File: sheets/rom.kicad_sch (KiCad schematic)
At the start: 3 parts, among them U34 NEO-E0, U35 74LS259, U36 27C1024

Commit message: Updated Footprints
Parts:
- U34: footprint (none) -> Package_LCC:PLCC-84
- U35: footprint (none) -> Package_DIP:DIP-16_W7.62mm
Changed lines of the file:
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@@
       (effects (font (size 1.27 1.27)) (justify left))
     )
-    (property "Footprint" "" (id 2) (at 156.21 93.218 0)
+    (property "Footprint" "Package_DIP:DIP-16_W7.62mm" (id 2) (at 156.21 93.218 0)
       (effects (font (size 1.27 1.27)) hide)
     )
@@
     (property "Reference" "U34" (id 0) (at 245.491 76.454 0))
     (property "Value" "NEO-E0" (id 1) (at 253.746 170.434 0))
-    (property "Footprint" "" (id 2) (at 253.746 136.144 0)
+    (property "Footprint" "Package_LCC:PLCC-84" (id 2) (at 253.746 136.144 0)
       (effects (font (size 1.27 1.27)) hide)
     )

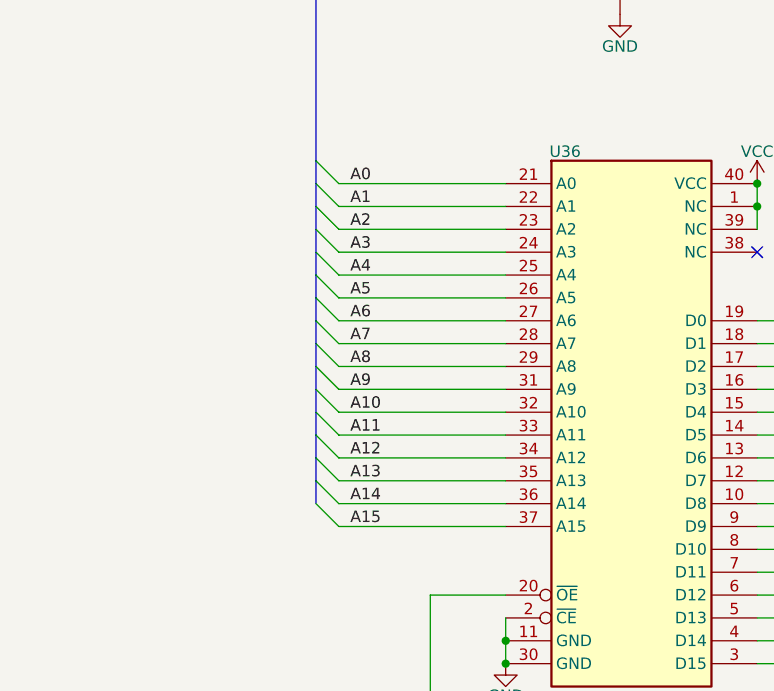
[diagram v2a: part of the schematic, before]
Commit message: Fix 27c1024 wrong address map
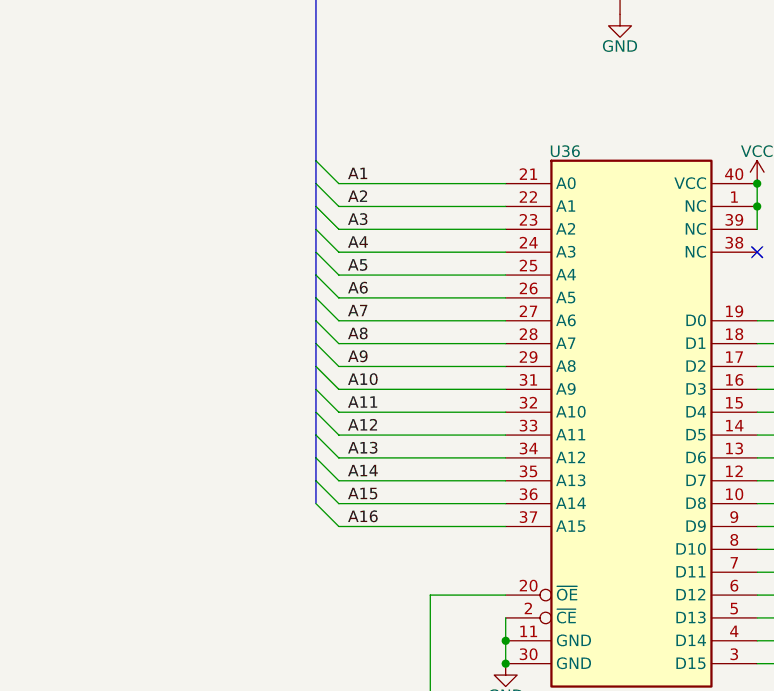
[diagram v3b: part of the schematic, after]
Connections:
- net A0 is gone; now on net A1: U36.21 (A0)
- net A1: no longer U36.22 (A1)
- net A10: now also U36.31 (A9); no longer U36.32 (A10)
- net A11: now also U36.32 (A10); no longer U36.33 (A11)
- net A12: now also U36.33 (A11); no longer U36.34 (A12)
- net A13: now also U36.34 (A12); no longer U36.35 (A13)
- net A14: now also U36.35 (A13); no longer U36.36 (A14)
- net A15: now also U36.36 (A14); no longer U36.37 (A15)
- net A16: now also U36.37 (A15)
- net A2: now also U36.22 (A1); no longer U36.23 (A2)
- net A3: now also U36.23 (A2); no longer U36.24 (A3)
- net A4: now also U36.24 (A3); no longer U36.25 (A4)
- net A5: now also U36.25 (A4); no longer U36.26 (A5)
- net A6: now also U36.26 (A5); no longer U36.27 (A6)
- net A7: now also U36.27 (A6); no longer U36.28 (A7)
- net A8: now also U36.28 (A7); no longer U36.29 (A8)
- net A9: now also U36.29 (A8); no longer U36.31 (A9)
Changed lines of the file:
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@@
     (stroke (width 0) (type default) (color 0 0 0 0))
   )
-  (label "A5" (at 126.238 142.494 0)
+  (label "A5" (at 125.984 139.954 0)
     (effects (font (size 1.27 1.27)) (justify left bottom))
   )
@@
     (effects (font (size 1.27 1.27)) (justify right bottom))
   )
-  (label "A2" (at 126.238 134.874 0)
+  (label "A2" (at 125.984 132.334 0)
     (effects (font (size 1.27 1.27)) (justify left bottom))
   )
@@
     (effects (font (size 1.27 1.27)) (justify right bottom))
   )
-  (label "A0" (at 126.238 129.794 0)
-    (effects (font (size 1.27 1.27)) (justify left bottom))
-  )
-  (label "A10" (at 126.238 155.194 0)
+  (label "A16" (at 125.984 167.894 0)
+    (effects (font (size 1.27 1.27)) (justify left bottom))
+  )
+  (label "A10" (at 125.984 152.654 0)
     (effects (font (size 1.27 1.27)) (justify left bottom))
   )
@@
     (effects (font (size 1.27 1.27)) (justify left bottom))
   )
-  (label "A12" (at 126.238 160.274 0)
+  (label "A12" (at 125.984 157.734 0)
     (effects (font (size 1.27 1.27)) (justify left bottom))
   )
@@
     (effects (font (size 1.27 1.27)) (justify left bottom))
   )
-  (label "A15" (at 126.238 167.894 0)
+  (label "A15" (at 125.984 165.354 0)
     (effects (font (size 1.27 1.27)) (justify left bottom))
   )
@@
     (effects (font (size 1.27 1.27)) (justify left bottom))
   )
-  (label "A9" (at 126.238 152.654 0)
+  (label "A9" (at 125.984 150.114 0)
     (effects (font (size 1.27 1.27)) (justify left bottom))
   )
@@
     (effects (font (size 1.27 1.27)) (justify left bottom))
   )
-  (label "A6" (at 126.238 145.034 0)
-    (effects (font (size 1.27 1.27)) (justify left bottom))
-  )
-  (label "A1" (at 126.238 132.334 0)
+  (label "A6" (at 125.984 142.494 0)
+    (effects (font (size 1.27 1.27)) (justify left bottom))
+  )
+  (label "A1" (at 125.984 129.794 0)
     (effects (font (size 1.27 1.27)) (justify left bottom))
   )
@@
     (effects (font (size 1.27 1.27)) (justify left bottom))
   )
-  (label "A11" (at 126.238 157.734 0)
+  (label "A11" (at 125.984 155.194 0)
     (effects (font (size 1.27 1.27)) (justify left bottom))
   )
@@
     (effects (font (size 1.27 1.27)) (justify right bottom))
   )
-  (label "A14" (at 126.238 165.354 0)
-    (effects (font (size 1.27 1.27)) (justify left bottom))
-  )
-  (label "A13" (at 126.238 162.814 0)
+  (label "A14" (at 125.984 162.814 0)
+    (effects (font (size 1.27 1.27)) (justify left bottom))
+  )
+  (label "A13" (at 125.984 160.274 0)
     (effects (font (size 1.27 1.27)) (justify left bottom))
   )
@@
     (effects (font (size 1.27 1.27)) (justify left bottom))
   )
-  (label "A4" (at 126.238 139.954 0)
+  (label "A4" (at 125.984 137.414 0)
     (effects (font (size 1.27 1.27)) (justify left bottom))
   )
@@
     (effects (font (size 1.27 1.27)) (justify right bottom))
   )
-  (label "A3" (at 126.238 137.414 0)
-    (effects (font (size 1.27 1.27)) (justify left bottom))
-  )
-  (label "A8" (at 126.238 150.114 0)
-    (effects (font (size 1.27 1.27)) (justify left bottom))
-  )
-  (label "A7" (at 126.238 147.574 0)
-    (effects (font (size 1.27 1.27)) (justify left bottom))
-  )
+  (label "A3" (at 125.984 134.874 0)
+    (effects (font (size 1.27 1.27)) (justify left bottom))
+  )
+  (label "A8" (at 125.984 147.574 0)
+    (effects (font (size 1.27 1.27)) (justify left bottom))
+  )
+  (label "A7" (at 125.984 145.034 0)
+    (effects (font (size 1.27 1.27)) (justify left bottom))
+  )

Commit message: Sync footprints from Nightly Build
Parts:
- U34: footprint Package_LCC:PLCC-84 -> 1_NeoGeoLibrary:NEO-G0
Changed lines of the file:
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@@
     (property "Reference" "U34" (id 0) (at 245.491 76.454 0))
     (property "Value" "NEO-E0" (id 1) (at 253.746 170.434 0))
-    (property "Footprint" "Package_LCC:PLCC-84" (id 2) (at 253.746 136.144 0)
+    (property "Footprint" "1_NeoGeoLibrary:NEO-G0" (id 2) (at 253.746 136.144 0)
       (effects (font (size 1.27 1.27)) hide)
     )

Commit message: Schematics Footprint updates
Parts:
- U35: footprint Package_DIP:DIP-16_W7.62mm -> 1_NeoGeoLibrary:DIP-16_W7.62mm
- U36: footprint Package_DIP:DIP-40_W15.24mm -> 1_NeoGeoLibrary:DIP-40_W15.24mm
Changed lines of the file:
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@@
       (effects (font (size 1.27 1.27)))
     )
-    (property "Footprint" "Package_DIP:DIP-40_W15.24mm" (at 157.48 192.024 0)
+    (property "Footprint" "1_NeoGeoLibrary:DIP-40_W15.24mm" (at 157.48 192.024 0)
       (effects (font (size 1.27 1.27)) hide)
     )
@@
       (effects (font (size 1.27 1.27)) (justify left))
     )
-    (property "Footprint" "Package_DIP:DIP-16_W7.62mm" (at 156.21 93.218 0)
+    (property "Footprint" "1_NeoGeoLibrary:DIP-16_W7.62mm" (at 156.21 93.218 0)
       (effects (font (size 1.27 1.27)) hide)
     )

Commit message: Some tweaks
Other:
- company: (none) -> SNK
- title: (none) -> NeoGeo AES
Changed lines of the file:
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@@
 (kicad_sch (version 20230121) (generator eeschema)
   (paper "A3")
+  (title_block
+    (title "NeoGeo AES")
+    (date "2023-08-19")
+    (rev "3.5")
+    (company "SNK")
+    (comment 3 "https://github.com/Board-Folk")
+    (comment 4 "Recreated By The Board Folk Team")
+  )
   (junction (at 143.51 180.594) (diameter 0) (color 0 0 0 0)
   )

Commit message: Updates to PCB Move P2 Joystick Port Move Memory Card Move Holes at top right Silkscreen added Update Titles
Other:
- title: NeoGeo AES -> NeoGeo AES 3-5
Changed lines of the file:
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@@
   (paper "A3")
   (title_block
-    (title "NeoGeo AES")
-    (date "2023-08-19")
-    (rev "3.5")
+    (title "NeoGeo AES 3-5")
+    (date "2023-08-27")
+    (rev "BF1.1")
     (company "SNK")
     (comment 3 "https://github.com/Board-Folk")
